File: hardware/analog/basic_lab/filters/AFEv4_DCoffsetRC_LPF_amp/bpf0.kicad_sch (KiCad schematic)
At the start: 4 parts, among them J3 Connector_Generic_Conn_01x02, J4 Connector_Generic_Conn_01x02

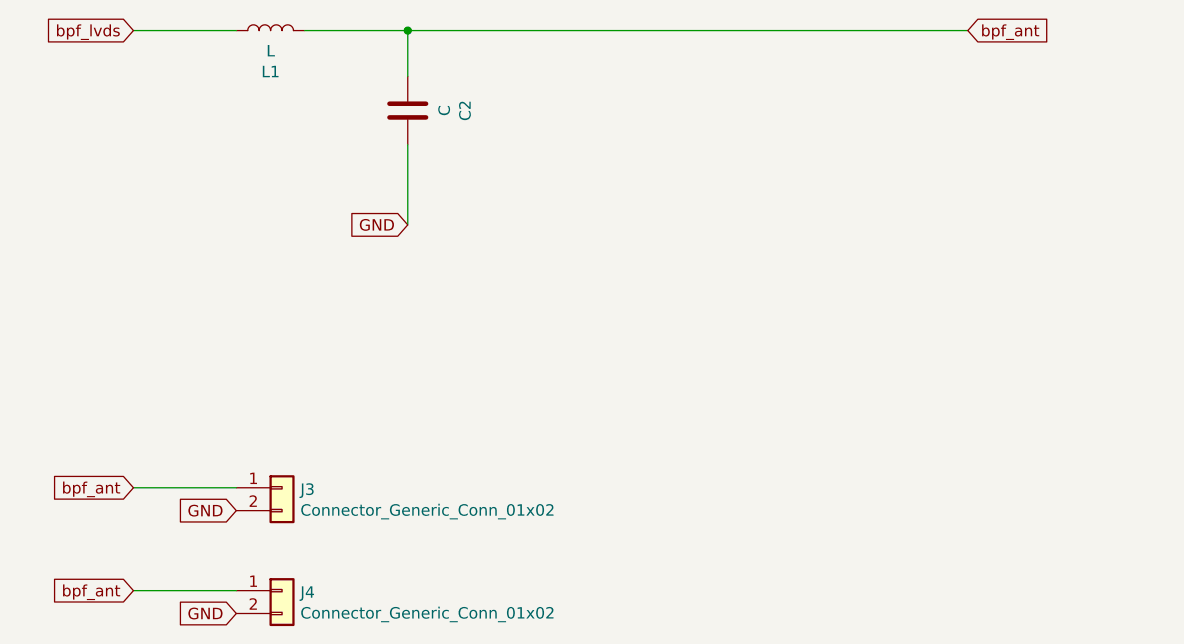
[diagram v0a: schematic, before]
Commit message: started PCB LVDS 1-bit AFE + BC547 amp + LC LPF filters
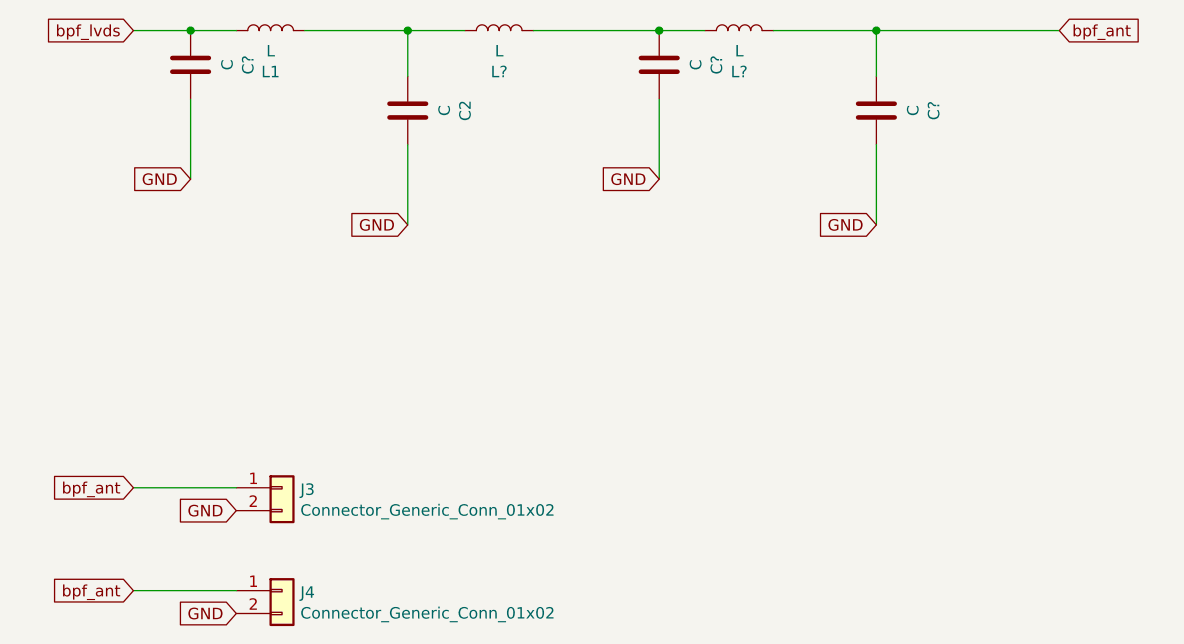
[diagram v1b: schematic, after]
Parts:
- added C? (x3): C, Capacitor_SMD:C_1206_3216Metric, symbol Device:C
- added L? (x2): L, Inductor_SMD:L_1206_3216Metric, symbol Device:L
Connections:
- net GND: now also C?.1, C?.1, C?.1
- net bpf_ant: now also C?.2, L?.2; no longer C2.2, L1.2
- net bpf_lvds: now also C?.2
- new net: C2.2, L1.2, L?.1
- new net: C?.2, L?.1, L?.2
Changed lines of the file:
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@@
   (junction (at 85.09 68.58) (diameter 0) (color 0 0 0 0)
   )
+  (junction (at 137.16 68.58) (diameter 0) (color 0 0 0 0)
+  )
+  (junction (at 113.03 68.58) (diameter 0) (color 0 0 0 0)
+  )
+  (junction (at 60.96 68.58) (diameter 0) (color 0 0 0 0)
+  )
   (wire (pts (xy 54.61 119.38) (xy 66.04 119.38))
     (stroke (width 0) (type default) (color 0 0 0 0))
@@
     (stroke (width 0) (type default) (color 0 0 0 0))
   )
+  (wire (pts (xy 60.96 68.58) (xy 54.61 68.58))
+    (stroke (width 0) (type default) (color 0 0 0 0))
+  )
   (wire (pts (xy 73.66 68.58) (xy 85.09 68.58))
     (stroke (width 0) (type default) (color 0 0 0 0))
   )
-  (wire (pts (xy 85.09 68.58) (xy 147.32 68.58))
+  (wire (pts (xy 118.11 68.58) (xy 113.03 68.58))
+    (stroke (width 0) (type default) (color 0 0 0 0))
+  )
+  (wire (pts (xy 85.09 68.58) (xy 91.44 68.58))
+    (stroke (width 0) (type default) (color 0 0 0 0))
+  )
+  (wire (pts (xy 137.16 81.28) (xy 137.16 90.17))
     (stroke (width 0) (type default) (color 0 0 0 0))
   )
@@
     (stroke (width 0) (type default) (color 0 0 0 0))
   )
-  (wire (pts (xy 66.04 68.58) (xy 54.61 68.58))
+  (wire (pts (xy 113.03 76.2) (xy 113.03 85.09))
+    (stroke (width 0) (type default) (color 0 0 0 0))
+  )
+  (wire (pts (xy 99.06 68.58) (xy 113.03 68.58))
+    (stroke (width 0) (type default) (color 0 0 0 0))
+  )
+  (wire (pts (xy 66.04 68.58) (xy 60.96 68.58))
+    (stroke (width 0) (type default) (color 0 0 0 0))
+  )
+  (wire (pts (xy 60.96 76.2) (xy 60.96 85.09))
+    (stroke (width 0) (type default) (color 0 0 0 0))
+  )
+  (wire (pts (xy 137.16 68.58) (xy 157.48 68.58))
+    (stroke (width 0) (type default) (color 0 0 0 0))
+  )
+  (wire (pts (xy 125.73 68.58) (xy 137.16 68.58))
+    (stroke (width 0) (type default) (color 0 0 0 0))
+  )
+  (wire (pts (xy 137.16 68.58) (xy 137.16 73.66))
     (stroke (width 0) (type default) (color 0 0 0 0))
   )
@@
     )
   )
-  (global_label "bpf_ant" (shape input) (at 147.32 68.58 0) (fields_autoplaced)
+  (global_label "GND" (shape input) (at 113.03 85.09 180) (fields_autoplaced)
+    (effects (font (size 1.27 1.27)) (justify right))
+    (property "Intersheet References" "${INTERSHEET_REFS}" (id 0) (at -17.78 26.67 0)
+      (effects (font (size 1.27 1.27)) hide)
+    )
+  )
+  (global_label "bpf_ant" (shape input) (at 157.48 68.58 0) (fields_autoplaced)
     (effects (font (size 1.27 1.27)) (justify left))
-    (property "Intersheet References" "${INTERSHEET_REFS}" (id 0) (at -69.85 -11.43 0)
+    (property "Intersheet References" "${INTERSHEET_REFS}" (id 0) (at -59.69 -11.43 0)
+      (effects (font (size 1.27 1.27)) hide)
+    )
+  )
+  (global_label "GND" (shape input) (at 60.96 85.09 180) (fields_autoplaced)
+    (effects (font (size 1.27 1.27)) (justify right))
+    (property "Intersheet References" "${INTERSHEET_REFS}" (id 0) (at -69.85 26.67 0)
       (effects (font (size 1.27 1.27)) hide)
     )
@@
     )
   )
+  (global_label "GND" (shape input) (at 137.16 90.17 180) (fields_autoplaced)
+    (effects (font (size 1.27 1.27)) (justify right))
+    (property "Intersheet References" "${INTERSHEET_REFS}" (id 0) (at 6.35 31.75 0)
+      (effects (font (size 1.27 1.27)) hide)
+    )
+  )
   (global_label "GND" (shape input) (at 85.09 90.17 180) (fields_autoplaced)
     (effects (font (size 1.27 1.27)) (justify right))
@@
       (effects (font (size 1.27 1.27)) hide)
     )
+  )
+  (symbol (lib_id "Device:C") (at 60.96 72.39 180) (unit 1)
+    (in_bom yes) (on_board yes)
+    (property "Reference" "C?" (id 0) (at 67.3608 72.39 90))
+    (property "Value" "C" (id 1) (at 65.0494 72.39 90))
+    (property "Footprint" "Capacitor_SMD:C_1206_3216Metric" (id 2) (at 59.9948 68.58 0)
+      (effects (font (size 1.27 1.27)) hide)
+    )
+    (property "Datasheet" "~" (id 3) (at 60.96 72.39 0)
+      (effects (font (size 1.27 1.27)) hide)
+    )
+    (pin "1")
+    (pin "2")
+  )
+  (symbol (lib_id "Device:L") (at 95.25 68.58 90) (unit 1)
+    (in_bom yes) (on_board yes)
+    (property "Reference" "L?" (id 0) (at 95.25 73.1774 90))
+    (property "Value" "L" (id 1) (at 95.25 70.866 90))
+    (property "Footprint" "Inductor_SMD:L_1206_3216Metric" (id 2) (at 95.25 68.58 0)
+      (effects (font (size 1.27 1.27)) hide)
+    )
+    (property "Datasheet" "~" (id 3) (at 95.25 68.58 0)
+      (effects (font (size 1.27 1.27)) hide)
+    )
+    (pin "1")
+    (pin "2")
   )
   (symbol (lib_id "Device:C") (at 85.09 77.47 180) (unit 1)
@@
       (effects (font (size 1.27 1.27)) hide)
     )
+    (pin "1")
+    (pin "2")
+  )
+  (symbol (lib_id "Device:C") (at 113.03 72.39 180) (unit 1)
+    (in_bom yes) (on_board yes)
+    (property "Reference" "C?" (id 0) (at 119.4308 72.39 90))
+    (property "Value" "C" (id 1) (at 117.1194 72.39 90))
+    (property "Footprint" "Capacitor_SMD:C_1206_3216Metric" (id 2) (at 112.0648 68.58 0)
+      (effects (font (size 1.27 1.27)) hide)
+    )
+    (property "Datasheet" "~" (id 3) (at 113.03 72.39 0)
+      (effects (font (size 1.27 1.27)) hide)
+    )
+    (pin "1")
+    (pin "2")
+  )
+  (symbol (lib_id "Device:L") (at 121.92 68.58 90) (unit 1)
+    (in_bom yes) (on_board yes)
+    (property "Reference" "L?" (id 0) (at 121.92 73.1774 90))
+    (property "Value" "L" (id 1) (at 121.92 70.866 90))
+    (property "Footprint" "Inductor_SMD:L_1206_3216Metric" (id 2) (at 121.92 68.58 0)
+      (effects (font (size 1.27 1.27)) hide)
+    )
+    (property "Datasheet" "~" (id 3) (at 121.92 68.58 0)
+      (effects (font (size 1.27 1.27)) hide)
+    )
+    (pin "1")
+    (pin "2")
+  )
+  (symbol (lib_id "Device:C") (at 137.16 77.47 180) (unit 1)
+    (in_bom yes) (on_board yes)
+    (property "Reference" "C?" (id 0) (at 143.5608 77.47 90))
+    (property "Value" "C" (id 1) (at 141.2494 77.47 90))
+    (property "Footprint" "Capacitor_SMD:C_1206_3216Metric" (id 2) (at 136.1948 73.66 0)
+      (effects (font (size 1.27 1.27)) hide)
+    )
+    (property "Datasheet" "~" (id 3) (at 137.16 77.47 0)
+      (effects (font (size 1.27 1.27)) hide)
+    )
